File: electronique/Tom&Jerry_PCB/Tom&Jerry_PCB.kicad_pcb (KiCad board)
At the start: 4 copper layers, 54 x 57 mm, 143 parts, among them IC1101 NCS199A2RSQT2G, IC301 TCA9555RTWR, IC901 NCS199A2RSQT2G, J1001 FTSH-105-01-F-DV-P-TR, J1301 Conn_01x02, J1501 Conn_01x02, J1601 Conn_01x02, J1701 Conn_01x02, J201 Interrupteur, J202 USB_C_Receptacle_USB2.0_16P, J203 Conn_01x02, J204 Conn_01x02, J301 Conn_01x08, J401 Conn_01x06, J402 Conn_01x06, J501 Conn_ST_STDC14, J601 Conn_01x03, J701 FTSH-105-01-F-DV-P-TR, Q201 SI2365EDS-T1-GE3, SW501 SW_Push, SW502 SW_Push, SW503 SW_Push, U1101 ZXBM5210-S, U201 MP1475DJ-LF-P, U202 BQ25172DSGR, U301 ADXL343, U501 STM32G431CBU6, U601 PAM8302AAY, U801 LP5812ADSDR, U901 ZXBM5210-S, Y501 16MHz

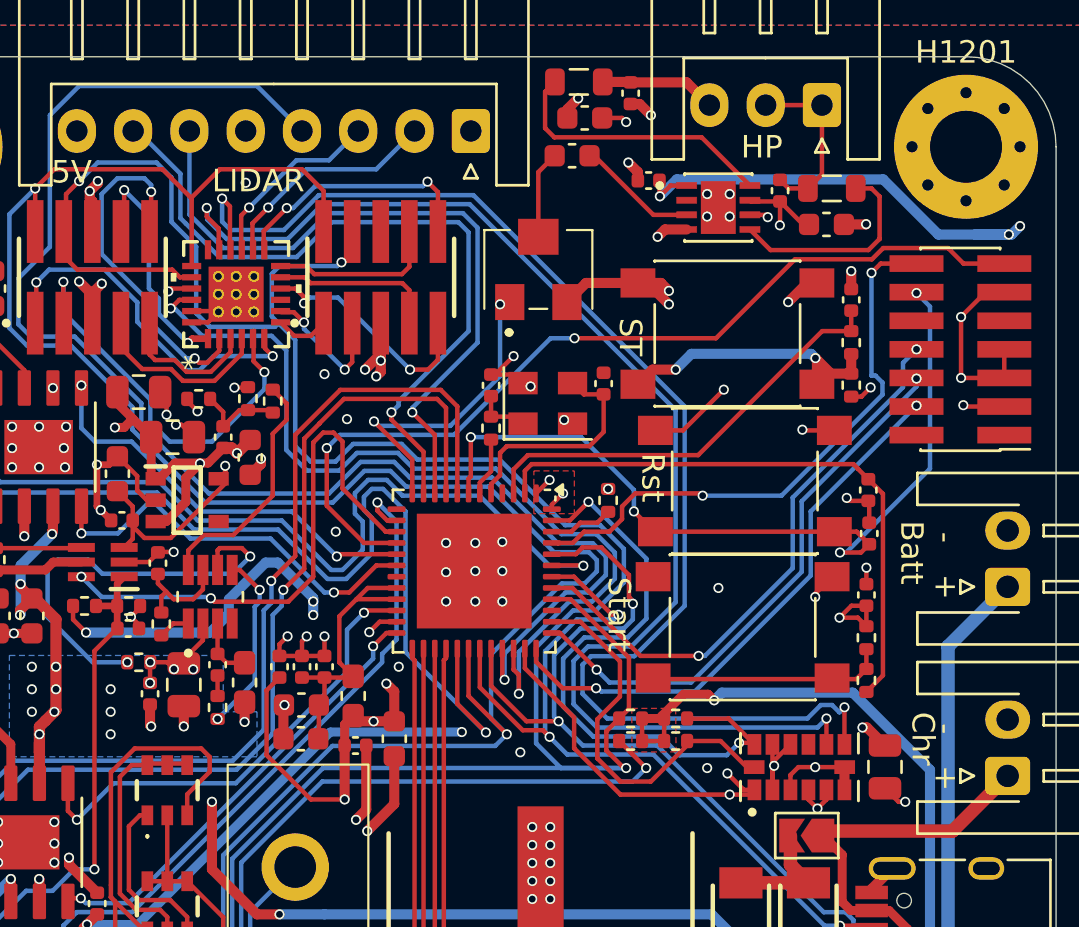
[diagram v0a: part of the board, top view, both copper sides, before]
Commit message: Correction erreurs PCB
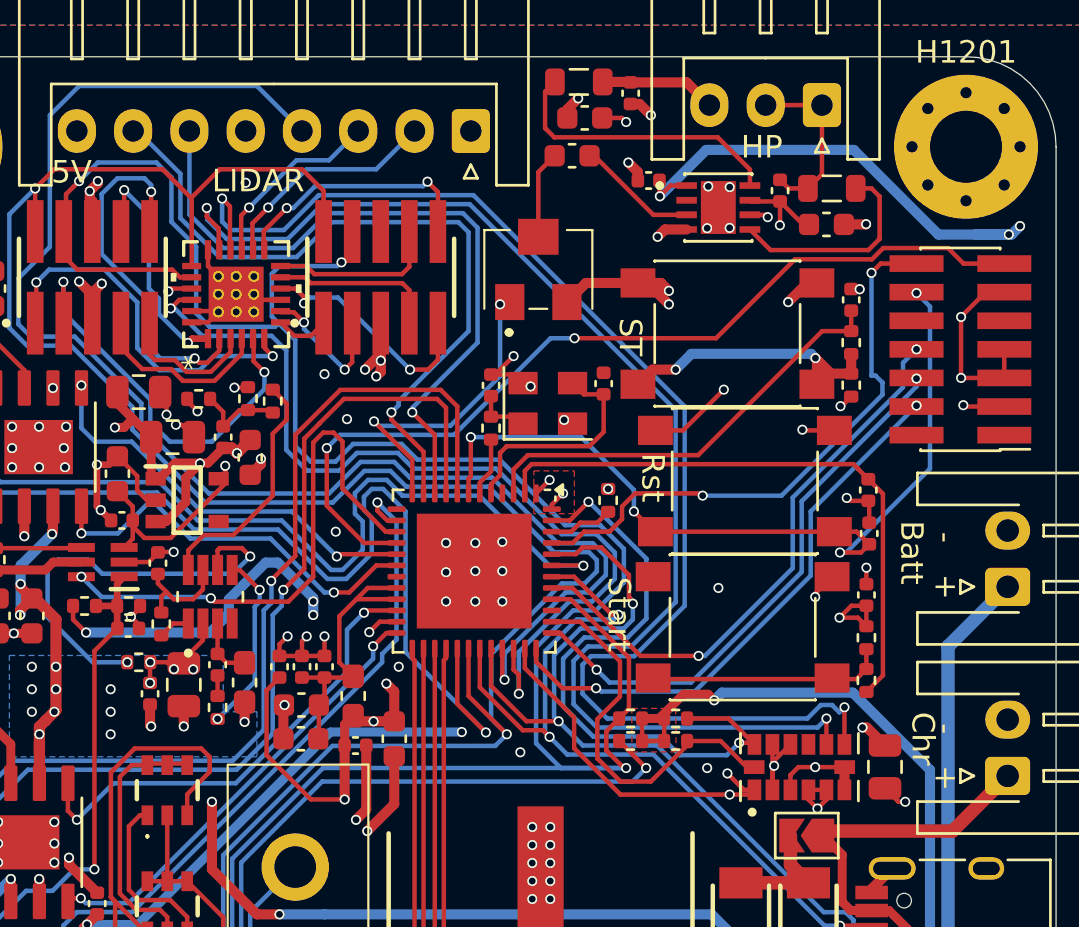
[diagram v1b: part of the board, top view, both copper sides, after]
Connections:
- IC301 pad 25: (no net) -> GND
- IC301 pad V: (no net) -> GND
- U1101 pad 9: (no net) -> GND
- U202 pad 10: (no net) -> GND
- U202 pad 11: (no net) -> GND
- U601 pad 9: (no net) -> GND
- U901 pad 9: (no net) -> GND
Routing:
- net GND: track 117.9 -> 121.0 mm
- net +3.3V: track 122.1 -> 122.8 mm
- net /Périphériques/TOF6_GPIO1: track 15.8 -> 16.4 mm
- net /Périphériques/TOF4_XSHUT: track 16.5 -> 17.1 mm

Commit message: Adding all files to critic error PCB
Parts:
- added C1: 10uF, Capacitor_SMD:C_0603_1608Metric, F.Cu at (79.2, 78.8)
- added C2: 10uF, Capacitor_SMD:C_0603_1608Metric, F.Cu at (78.7, 96.7)
- added C302: 0.1u, Capacitor_SMD:C_0603_1608Metric, F.Cu at (120.5, 89.2)
- C301: footprint Capacitor_SMD:C_0805_2012Metric -> Capacitor_SMD:C_0402_1005Metric
- R209: value R_Small -> 3.3k
- moved C507 19.0 mm to (101.9, 72.0)
- moved C511 15.3 mm to (107.0, 76.5), turned to -90 degrees
- moved C510 13.8 mm to (107.0, 87.0), turned to -90 degrees
- moved C301 6.64 mm to (114.5, 92.0)
- moved C512 3.29 mm to (96.5, 83.2), turned to -90 degrees
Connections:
- IC301 pad 25: GND -> (no net)
- IC301 pad V: GND -> (no net)
- U1101 pad 9: GND -> (no net)
- U202 pad 10: GND -> (no net)
- U202 pad 11: GND -> (no net)
- U601 pad 9: GND -> (no net)
- U901 pad 9: GND -> (no net)
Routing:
- net VCC: track 54.8 -> 61.4 mm, vias 10 -> 12
- net /STM32/NRST: track 37.9 -> 36.4 mm
- net +3.3VA: track 12.9 -> 13.6 mm, vias 0 -> 2
- net Net-(U201-EN/SYNC): track 18.8 -> 19.4 mm
- net GND: track 121.0 -> 121.2 mm, vias 102 -> 104
- net +3.3V: vias 28 -> 27
- net +5V: vias 35 -> 34
- added copper zone on F.Cu, net +3.3VA
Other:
- board text removed: "GND"

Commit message: Last commit before PCB command
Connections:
- IC301 pad 25: (no net) -> GND
- IC301 pad V: (no net) -> GND
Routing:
- net +3.3V: track 122.8 -> 114.3 mm
- net GND: track 121.2 -> 122.4 mm

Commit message: Derniere modif jlcpcb
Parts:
- R1101, R901: footprint Resistor_SMD:R_0402_1005Metric -> Resistor_SMD:R_0805_2012Metric
- moved C1102 2.05 mm to (83.3, 84.1), turned to 45 degrees
- moved R1101 1.94 mm to (82.0, 81.3), turned to -45 degrees
- moved C903 1.52 mm to (80.9, 101.2), turned to 0 degrees
- moved C1103 0.93 mm to (81.0, 83.2), turned to -45 degrees
- moved R901 0.39 mm to (80.4, 97.7)
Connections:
- U1101 pad 9: (no net) -> GND
- U202 pad 10: (no net) -> GND
- U202 pad 11: (no net) -> GND
- U601 pad 9: (no net) -> GND
- U901 pad 9: (no net) -> GND
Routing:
- net /Motors&Drivers/Motor1+: track 7.78 -> 11.8 mm
- net +5V: track 120.5 -> 117.8 mm, vias 34 -> 30
- net GND: track 122.4 -> 124.6 mm, vias 104 -> 101
- net Net-(IC1101-IN+): track 5.68 -> 7.19 mm
